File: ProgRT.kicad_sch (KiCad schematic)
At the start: 68 parts

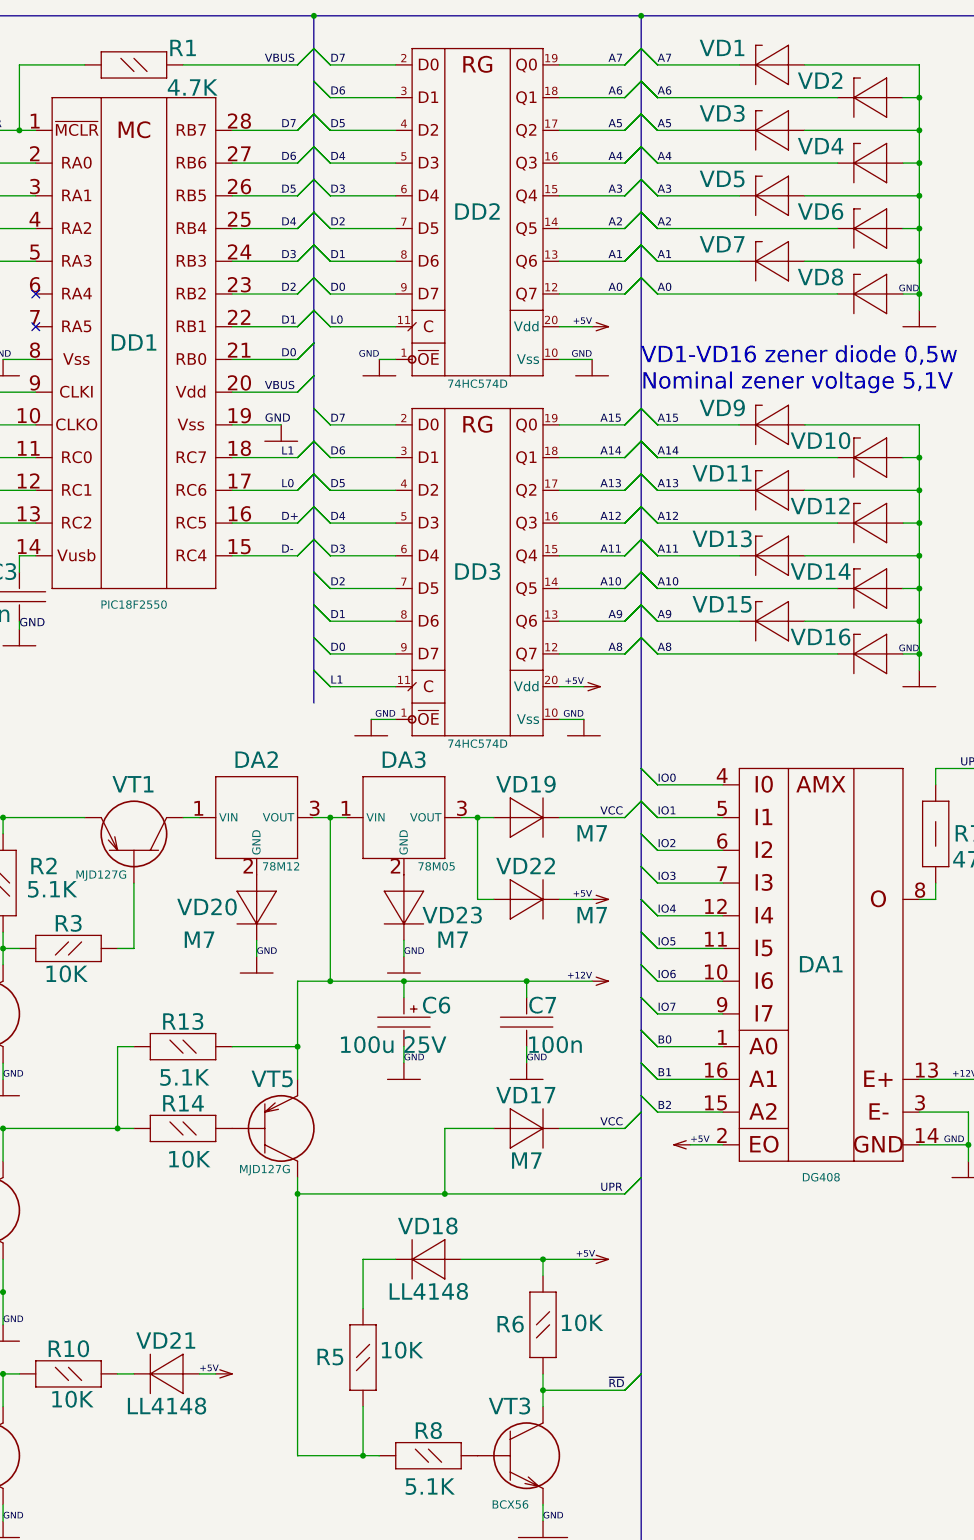
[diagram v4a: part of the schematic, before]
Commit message: Fix diodes on silk screen
Diodes were reversed because pin numbers got corrupted during import. Fix them,
so that silk screen and fab layer is displayed correctly
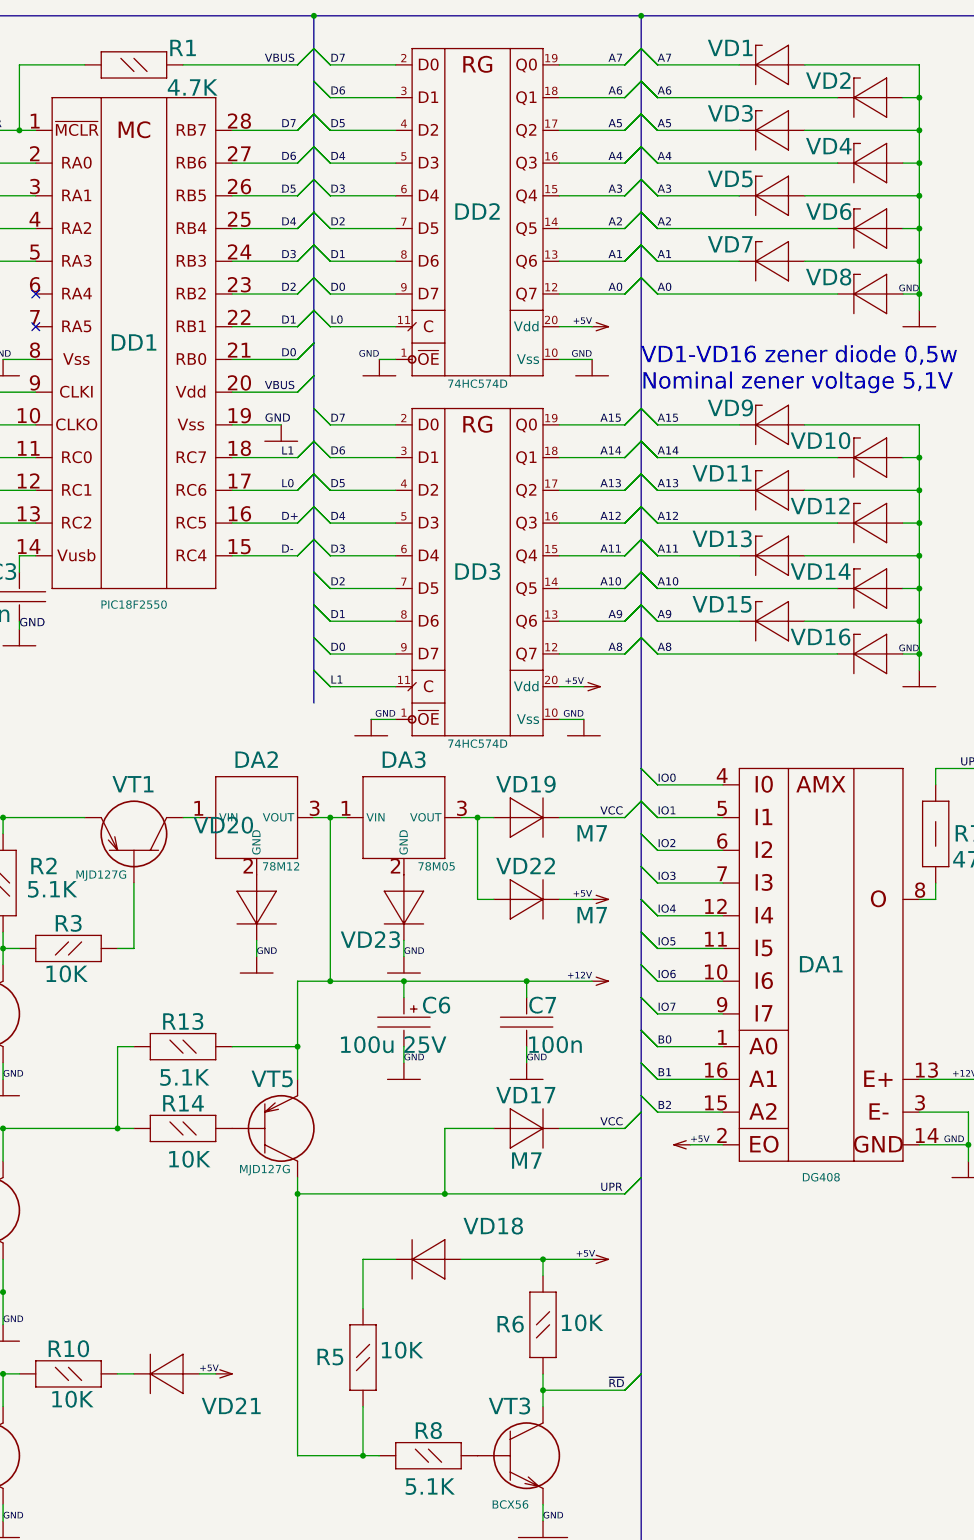
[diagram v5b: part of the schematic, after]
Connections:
- net +5V: now also VD18.2 (A), VD21.2 (A), VD22.1 (C), VD24.2 (A), VD25.2 (A); no longer VD18.1 (A), VD21.1 (A), VD22.2 (C), VD24.1 (A), VD25.1 (A)
- net A0: now also VD8.1 (C); no longer VD8.2 (C)
- net A1: now also VD7.1 (C); no longer VD7.2 (C)
- net A10: now also VD14.1 (C); no longer VD14.2 (C)
- net A11: now also VD13.1 (C); no longer VD13.2 (C)
- net A12: now also VD12.1 (C); no longer VD12.2 (C)
- net A13: now also VD11.1 (C); no longer VD11.2 (C)
- net A14: now also VD10.1 (C); no longer VD10.2 (C)
- net A15: now also VD9.1 (C); no longer VD9.2 (C)
- net A2: now also VD6.1 (C); no longer VD6.2 (C)
- net A3: now also VD5.1 (C); no longer VD5.2 (C)
- net A4: now also VD4.1 (C); no longer VD4.2 (C)
- net A5: now also VD3.1 (C); no longer VD3.2 (C)
- net A6: now also VD2.1 (C); no longer VD2.2 (C)
- net A7: now also VD1.1 (C); no longer VD1.2 (C)
- net A8: now also VD16.1 (C); no longer VD16.2 (C)
- net A9: now also VD15.1 (C); no longer VD15.2 (C)
- net GND: now also VD1.2 (A), VD10.2 (A), VD11.2 (A), VD12.2 (A), VD13.2 (A), VD14.2 (A), VD15.2 (A), VD16.2 (A), VD2.2 (A), VD20.1 (C), VD23.1 (C), VD3.2 (A), VD4.2 (A), VD5.2 (A), VD6.2 (A), VD7.2 (A), VD8.2 (A), VD9.2 (A); no longer VD1.1 (A), VD10.1 (A), VD11.1 (A), VD12.1 (A), VD13.1 (A), VD14.1 (A), VD15.1 (A), VD16.1 (A), VD2.1 (A), VD20.2 (C), VD23.2 (C), VD3.1 (A), VD4.1 (A), VD5.1 (A), VD6.1 (A), VD7.1 (A), VD8.1 (A), VD9.1 (A)
- net UPR: now also VD17.2 (A); no longer VD17.1 (A)
- net VCC: now also VD17.1 (C), VD19.1 (C); no longer VD17.2 (C), VD19.2 (C)
- net at DA2.2 (GND): now also VD20.2 (A); no longer VD20.1 (A)
- net at R12.1: now also VD25.1 (C); no longer VD25.2 (C)
- net at R9.2: now also VD24.1 (C); no longer VD24.2 (C)
- net at R5.2: now also VD18.1 (C); no longer VD18.2 (C)
- net at R10.2: now also VD21.1 (C); no longer VD21.2 (C)
- net at DA3.2 (GND): now also VD23.2 (A); no longer VD23.1 (A)
- new net: DA3.3 (VOUT), VD19.2 (A), VD22.2 (A)

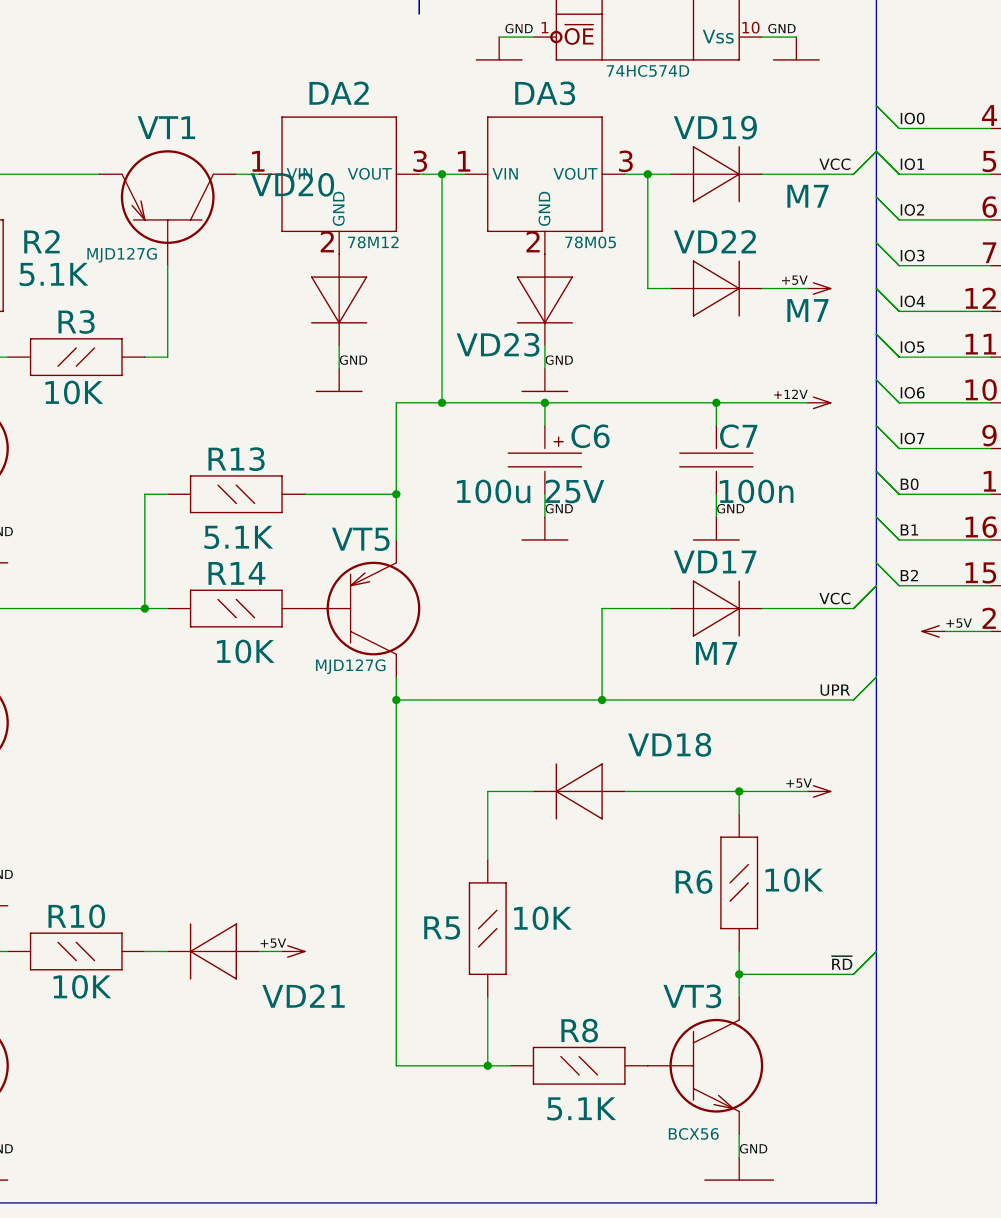
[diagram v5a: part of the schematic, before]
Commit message: Some fixups
- Finally remove the missing "empty" frame file
- Bring back diode types after pins fixup
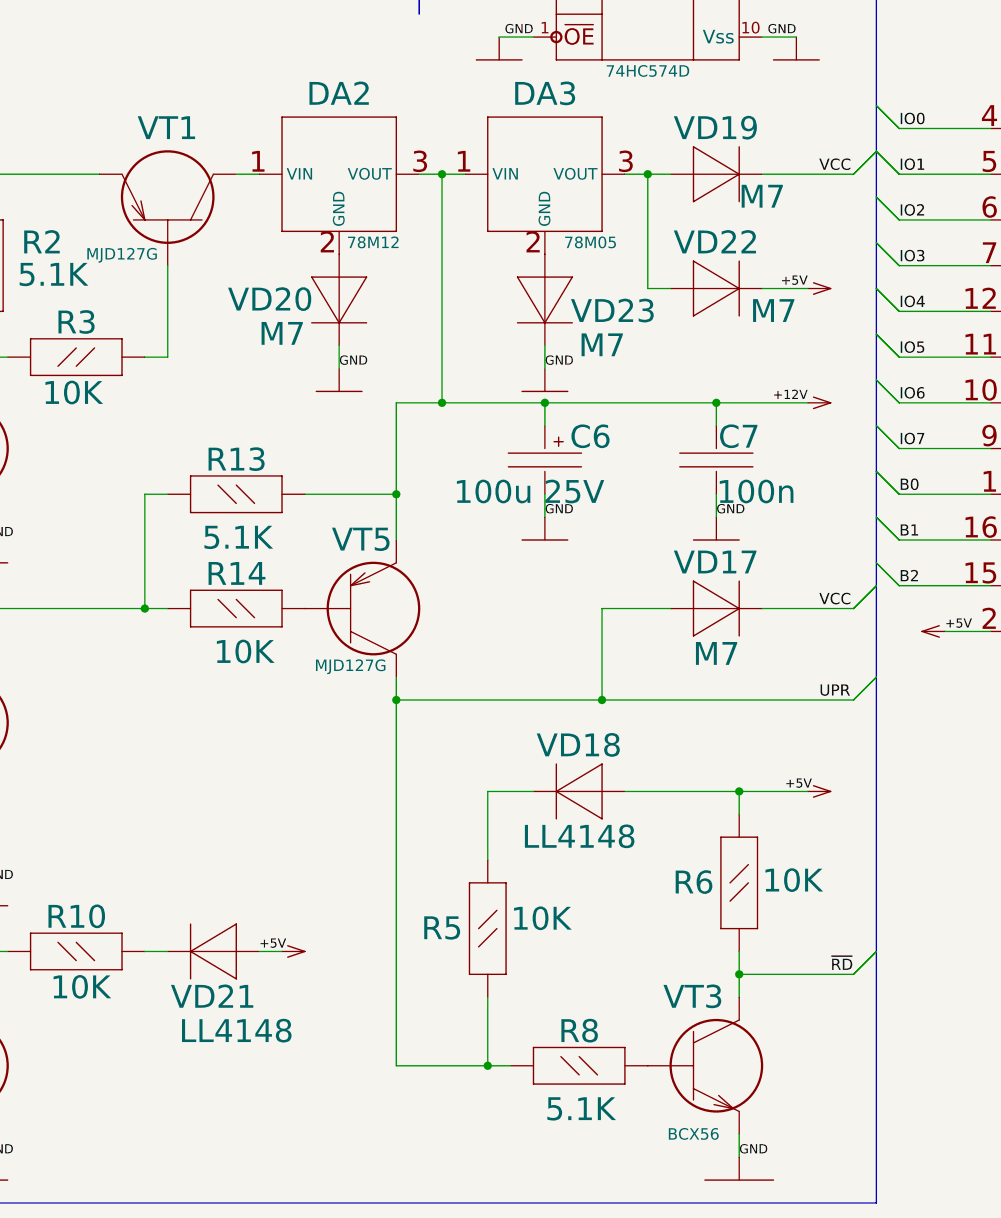
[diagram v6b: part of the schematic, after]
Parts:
- VD18, VD21: value КД522 -> LL4148
- VD20: value 1N400X -> M7
- VD23: value 1N400X -> (none)
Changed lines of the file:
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@@
       (effects (font (size 2.54 2.54)))
     )
-    (property "Value" "M7" (id 1) (at 187.96 165.1 0)
+    (property "Value" "M7" (id 1) (at 182.88 165.1 0)
       (effects (font (size 2.54 2.54)))
     )
@@
       (effects (font (size 1.27 1.27)) hide)
     )
-    (pin "2")
-    (pin "1")
+    (pin "1")
+    (pin "2")
   )
   (symbol (lib_name "1533IR37_1_2") (lib_id "ProgRT-eagle-import:1533IR37_1") (at 157.48 101.6 0) (unit 1)
@@
       (effects (font (size 1.27 1.27)) hide)
     )
-    (pin "2")
-    (pin "1")
+    (pin "1")
+    (pin "2")
   )
   (symbol (lib_name "1533IR37_1_2") (lib_id "ProgRT-eagle-import:1533IR37_1") (at 157.48 45.72 0) (unit 1)
@@
       (effects (font (size 2.54 2.54)))
     )
-    (property "Value" "M7" (id 1) (at 187.96 177.8 0)
+    (property "Value" "M7" (id 1) (at 184.15 177.8 0)
       (effects (font (size 2.54 2.54)))
     )
@@
   (symbol (lib_name "KD522_B_1_1") (lib_id "ProgRT-eagle-import:KD522_B_1") (at 167.64 231.14 0) (mirror y) (unit 1)
     (in_bom yes) (on_board yes)
-    (property "Reference" "VD18" (id 0) (at 172.72 226.06 0)
-      (effects (font (size 2.54 2.54)))
-    )
-    (property "Value" "LL4148" (id 1) (at 172.72 236.22 0)
-      (effects (font (size 2.54 2.54)) hide)
+    (property "Reference" "VD18" (id 0) (at 162.56 226.06 0)
+      (effects (font (size 2.54 2.54)))
+    )
+    (property "Value" "LL4148" (id 1) (at 162.56 236.22 0)
+      (effects (font (size 2.54 2.54)))
     )
     (property "Footprint" "Diode_SMD:D_SMA" (id 2) (at 162.56 222.25 0)
@@
     (property "Datasheet" "" (id 3) (at 167.64 231.14 0)
       (effects (font (size 1.27 1.27)) hide)
-    )
-    (property "Value" "КД522" (id 4) (at 162.56 236.22 0)
-      (effects (font (size 2.54 2.54)) hide)
     )
     (pin "1")
@@
   (symbol (lib_id "ProgRT-eagle-import:KD522_B_1") (at 127 248.92 180) (unit 1)
     (in_bom yes) (on_board yes)
-    (property "Reference" "VD21" (id 0) (at 132.08 254 0)
-      (effects (font (size 2.54 2.54)))
-    )
-    (property "Value" "LL4148" (id 1) (at 132.08 254 0)
-      (effects (font (size 2.54 2.54)) hide)
+    (property "Reference" "VD21" (id 0) (at 121.92 254 0)
+      (effects (font (size 2.54 2.54)))
+    )
+    (property "Value" "LL4148" (id 1) (at 124.46 257.81 0)
+      (effects (font (size 2.54 2.54)))
     )
     (property "Footprint" "Diode_SMD:D_SMA" (id 2) (at 121.92 259.08 0)
@@
       (effects (font (size 1.27 1.27)) hide)
     )
-    (property "Value" "КД522" (id 4) (at 121.92 243.84 0)
-      (effects (font (size 2.54 2.54)) hide)
-    )
-    (pin "2")
-    (pin "1")
+    (pin "1")
+    (pin "2")
   )
   (symbol (lib_name "GND_1_1") (lib_id "ProgRT-eagle-import:GND_1") (at 238.76 83.82 0) (unit 1)
@@
   (symbol (lib_name "1N400X_B_1_3") (lib_id "ProgRT-eagle-import:1N400X_B_1") (at 158.75 171.45 270) (unit 1)
     (in_bom yes) (on_board yes)
-    (property "Reference" "VD23" (id 0) (at 153.67 181.61 90)
-      (effects (font (size 2.54 2.54)))
-    )
-    (property "Value" "M7" (id 1) (at 153.67 166.37 0)
-      (effects (font (size 2.54 2.54)) hide)
+    (property "Reference" "VD23" (id 0) (at 166.37 177.8 90)
+      (effects (font (size 2.54 2.54)))
+    )
+    (property "Value" "M7" (id 1) (at 165.1 181.61 90)
+      (effects (font (size 2.54 2.54)))
     )
     (property "Footprint" "Diode_SMD:D_SMA" (id 2) (at 163.83 175.26 0)
@@
       (effects (font (size 1.27 1.27)) hide)
     )
-    (property "Value" "1N400X" (id 4) (at 153.67 176.53 0)
+    (property "Value" "" (id 4) (at 153.67 176.53 0)
       (effects (font (size 2.54 2.54)) hide)
     )
@@
   (symbol (lib_name "1N400X_B_1_4") (lib_id "ProgRT-eagle-import:1N400X_B_1") (at 135.89 171.45 270) (unit 1)
     (in_bom yes) (on_board yes)
-    (property "Reference" "VD20" (id 0) (at 130.81 163.83 90)
-      (effects (font (size 2.54 2.54)))
-    )
-    (property "Value" "M7" (id 1) (at 129.54 173.99 0)
-      (effects (font (size 2.54 2.54)) hide)
+    (property "Reference" "VD20" (id 0) (at 128.27 176.53 90)
+      (effects (font (size 2.54 2.54)))
+    )
+    (property "Value" "M7" (id 1) (at 129.54 180.34 90)
+      (effects (font (size 2.54 2.54)))
     )
     (property "Footprint" "Diode_SMD:D_SMA" (id 2) (at 140.97 176.53 0)
@@
       (effects (font (size 1.27 1.27)) hide)
     )
-    (property "Value" "1N400X" (id 4) (at 130.81 176.53 0)
-      (effects (font (size 2.54 2.54)) hide)
-    )
-    (pin "1")
+    (pin "1")
